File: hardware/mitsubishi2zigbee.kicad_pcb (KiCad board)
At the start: 2 copper layers, 10 parts, among them J1 CN105, Q1 BSS138, Q2 BSS138

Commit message: refactor(kicad-pcb): tweak plot configuration and output directory
- update layerselection and plot_on_all_layers_selection masks
- adjust PDF metadata and popup settings
- modify outputdirectory to target location
- change drillshape, mirror, and outputformat values
- relocate drawing element to Edge.Cuts layer with new UUID
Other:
- board outline added: 30 x 45 mm
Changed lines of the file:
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@@
 		(filling no)
 		(pcbplotparams
-			(layerselection 0x00000000_00000000_55555555_5755f5ff)
-			(plot_on_all_layers_selection 0x00000000_00000000_00000000_00000000)
+			(layerselection 0x00000000_00000000_55555555_55555551)
+			(plot_on_all_layers_selection 0x00000000_00000000_00000000_02000000)
 			(disableapertmacros no)
 			(usegerberextensions no)
@@
 			(mode 1)
 			(useauxorigin no)
-			(pdf_front_fp_property_popups yes)
-			(pdf_back_fp_property_popups yes)
-			(pdf_metadata yes)
-			(pdf_single_document no)
+			(pdf_front_fp_property_popups no)
+			(pdf_back_fp_property_popups no)
+			(pdf_metadata no)
+			(pdf_single_document yes)
 			(dxfpolygonmode yes)
 			(dxfimperialunits yes)
@@
 			(crossoutdnponfab yes)
 			(subtractmaskfromsilk no)
-			(outputformat 1)
-			(mirror no)
-			(drillshape 1)
+			(outputformat 4)
+			(mirror yes)
+			(drillshape 0)
 			(scaleselection 1)
-			(outputdirectory "")
+			(outputdirectory "/home/cleboost/Downloads/")
 		)
 	)
@@
 	)
 	(gr_rect
-		(start 110 30)
-		(end 140 75)
+		(start 111 30.5)
+		(end 141 75.5)
 		(stroke
 			(width 0.1)
@@
 		)
 		(fill no)
-		(layer "Dwgs.User")
+		(layer "Edge.Cuts")
 	)
 	(segment

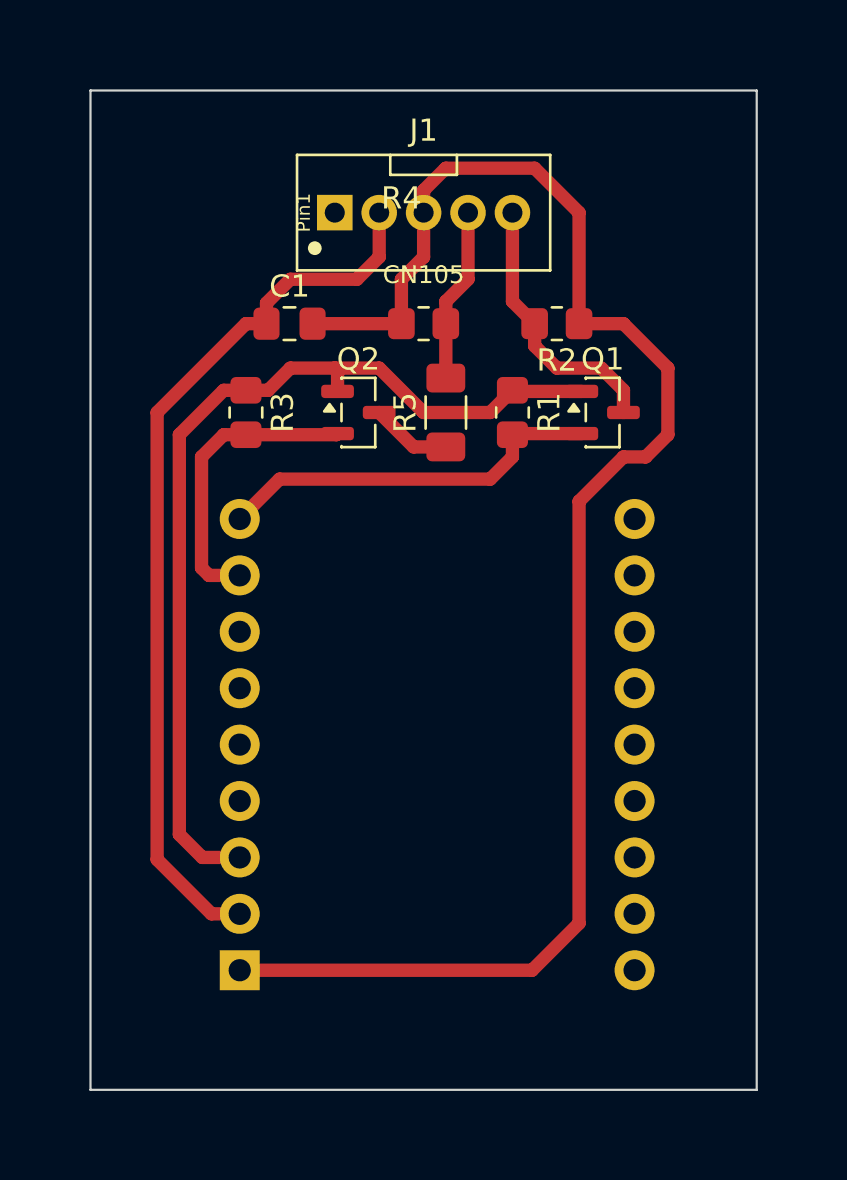
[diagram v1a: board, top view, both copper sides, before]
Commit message: fix(pcb): correct U1 pitch to 15.24mm and adapt pads for DIY etching/drilling
- Correct ESP32-C6-Zero footprint pitch from 17.78mm to official 15.24mm
- Reroute VCC trace around pin headers to ensure proper clearance
- Enlarge U1 pads to 2.1mm (0.9mm drill) for manual Dremel drilling
- Enlarge J1 pads to 1.5x2.2mm oval (0.8mm drill) and add 1.1mm boss hole
- Maintain 100% single-face F.Cu routing with 0 DRC/ERC errors
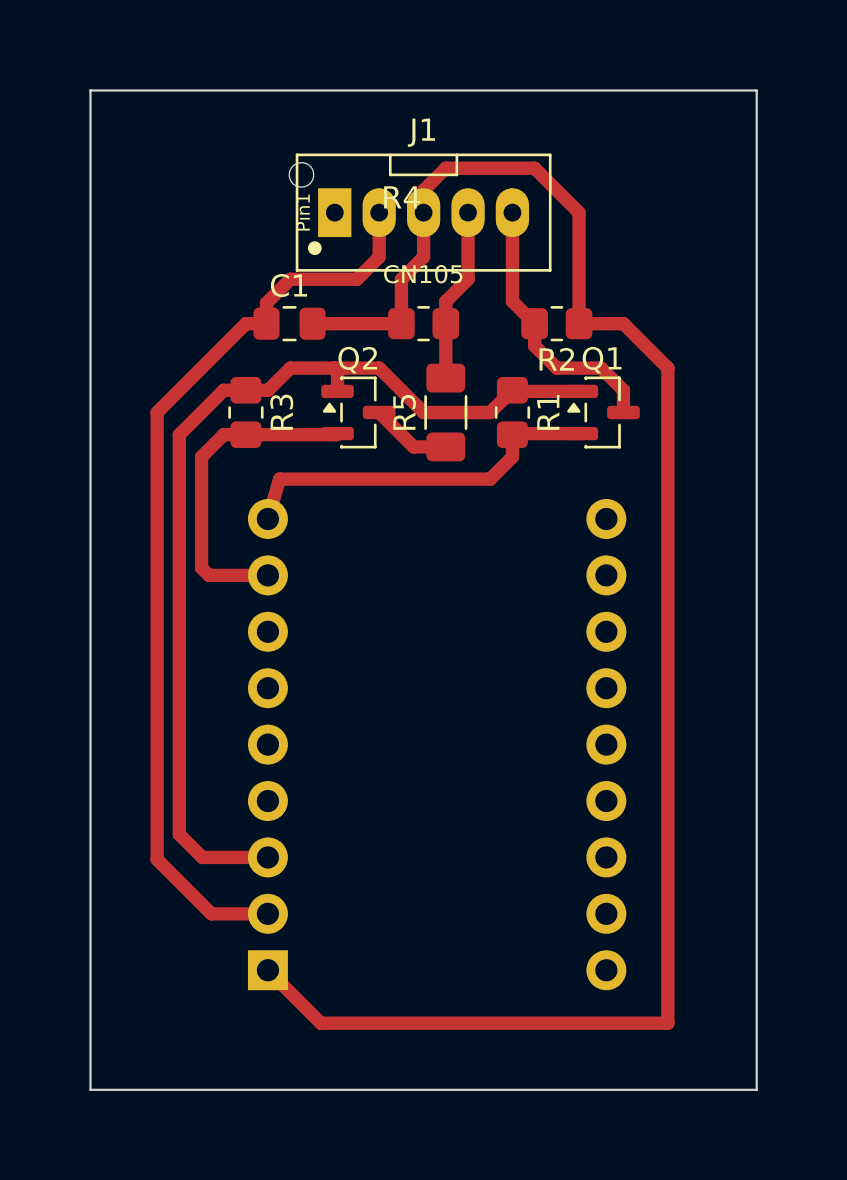
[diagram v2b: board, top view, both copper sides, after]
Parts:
- U1: value ~ -> ESP32-C6-Zero
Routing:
- net VCC: track 72.3 -> 77.4 mm
- net GND: track 40.4 -> 41.6 mm
- net /TX_3V3: track 13.4 -> 14.7 mm
- net +3V3: track 43.0 -> 44.2 mm
- net /RX_3V3: track 17.6 -> 16.9 mm
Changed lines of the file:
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@@
 			)
+		)
+		(pad "" np_thru_hole circle
+			(at -1.5 -1.7)
+			(size 1.1 1.1)
+			(drill 1.1)
+			(layers "*.Cu" "*.Mask")
 		)
 		(pad "1" thru_hole rect
 			(at 0 0)
-			(size 1.6 1.6)
-			(drill 0.9)
+			(size 1.5 2.2)
+			(drill 0.8)
 			(layers "*.Cu" "*.Mask")
 			(remove_unused_layers no)
@@
 		(pad "2" thru_hole oval
 			(at 2 0)
-			(size 1.6 1.6)
-			(drill 0.9)
+			(size 1.5 2.2)
+			(drill 0.8)
 			(layers "*.Cu" "*.Mask")
 			(remove_unused_layers no)
@@
 		(pad "3" thru_hole oval
 			(at 4 0)
-			(size 1.6 1.6)
-			(drill 0.9)
+			(size 1.5 2.2)
+			(drill 0.8)
 			(layers "*.Cu" "*.Mask")
 			(remove_unused_layers no)
@@
 		(pad "4" thru_hole oval
 			(at 6 0)
-			(size 1.6 1.6)
-			(drill 0.9)
+			(size 1.5 2.2)
+			(drill 0.8)
 			(layers "*.Cu" "*.Mask")
 			(remove_unused_layers no)
@@
 		(pad "5" thru_hole oval
 			(at 8 0)
-			(size 1.6 1.6)
-			(drill 0.9)
+			(size 1.5 2.2)
+			(drill 0.8)
 			(layers "*.Cu" "*.Mask")
 			(remove_unused_layers no)
@@
 			)
 		)
-		(property "Value" "~"
+		(property "Value" "ESP32-C6-Zero"
 			(at 0 -25 0)
 			(layer "B.Fab")
@@
 		)
 		(pad "1" thru_hole rect
-			(at -8.89 0)
+			(at -7.62 0)
 			(size 1.8 1.8)
 			(drill 1)
@@
 		)
 		(pad "2" thru_hole circle
-			(at -8.89 -2.54)
+			(at -7.62 -2.54)
 			(size 1.8 1.8)
 			(drill 1)
@@
 		)
 		(pad "3" thru_hole circle
-			(at -8.89 -5.08)
+			(at -7.62 -5.08)
 			(size 1.8 1.8)
 			(drill 1)
@@
 		)
 		(pad "4" thru_hole circle
-			(at -8.89 -7.62)
+			(at -7.62 -7.62)
 			(size 1.8 1.8)
 			(drill 1)
@@
 		)
 		(pad "5" thru_hole circle
-			(at -8.89 -10.16)
+			(at -7.62 -10.16)
 			(size 1.8 1.8)
 			(drill 1)
@@
 		)
 		(pad "6" thru_hole circle
-			(at -8.89 -12.7)
+			(at -7.62 -12.7)
 			(size 1.8 1.8)
 			(drill 1)
@@
 		)
 		(pad "7" thru_hole circle
-			(at -8.89 -15.24)
+			(at -7.62 -15.24)
 			(size 1.8 1.8)
 			(drill 1)
@@
 		)
 		(pad "8" thru_hole circle
-			(at -8.89 -17.78)
+			(at -7.62 -17.78)
 			(size 1.8 1.8)
 			(drill 1)
@@
 		)
 		(pad "9" thru_hole circle
-			(at -8.89 -20.32)
+			(at -7.62 -20.32)
 			(size 1.8 1.8)
 			(drill 1)
@@
 		)
 		(pad "10" thru_hole circle
-			(at 8.89 -20.32)
+			(at 7.62 -20.32)
 			(size 1.8 1.8)
 			(drill 1)
@@
 		)
 		(pad "11" thru_hole circle
-			(at 8.89 -17.78)
+			(at 7.62 -17.78)
 			(size 1.8 1.8)
 			(drill 1)
@@
 		)
 		(pad "12" thru_hole circle
-			(at 8.89 -15.24)
+			(at 7.62 -15.24)
 			(size 1.8 1.8)
 			(drill 1)
@@
 		)
 		(pad "13" thru_hole circle
-			(at 8.89 -12.7)
+			(at 7.62 -12.7)
 			(size 1.8 1.8)
 			(drill 1)
@@
 		)
 		(pad "14" thru_hole circle
-			(at 8.89 -10.16)
+			(at 7.62 -10.16)
 			(size 1.8 1.8)
 			(drill 1)
@@
 		)
 		(pad "15" thru_hole circle
-			(at 8.89 -7.62)
+			(at 7.62 -7.62)
 			(size 1.8 1.8)
 			(drill 1)
@@
 		)
 		(pad "16" thru_hole circle
-			(at 8.89 -5.08)
+			(at 7.62 -5.08)
 			(size 1.8 1.8)
 			(drill 1)
@@
 		)
 		(pad "17" thru_hole circle
-			(at 8.89 -2.54)
+			(at 7.62 -2.54)
 			(size 1.8 1.8)
 			(drill 1)
@@
 		)
 		(pad "18" thru_hole circle
-			(at 8.89 0)
+			(at 7.62 0)
 			(size 1.8 1.8)
 			(drill 1)
@@
 	)
 	(segment
-		(start 117.72 65.035)
+		(start 118.99 65.035)
 		(end 116.035 65.035)
 		(width 0.6)
@@
 	(segment
 		(start 119.515 48)
-		(end 117.72 49.795)
+		(end 118.99 49.795)
 		(width 0.6)
 		(layer "F.Cu")
@@
 	)
 	(segment
+		(start 137 43)
+		(end 137 72.5)
+		(width 0.6)
+		(layer "F.Cu")
+		(net "VCC")
+	)
+	(segment
 		(start 121 41)
 		(end 125 41)
@@
 	)
 	(segment
-		(start 135 47)
-		(end 136 47)
+		(start 125 41)
+		(end 124.73 40.73)
+		(width 0.6)
+		(layer "F.Cu")
+		(net "VCC")
+	)
+	(segment
+		(start 125 39)
+		(end 125 41)
+		(width 0.6)
+		(layer "F.Cu")
+		(net "VCC")
+	)
+	(segment
+		(start 126 38)
+		(end 125 39)
+		(width 0.6)
+		(layer "F.Cu")
+		(net "VCC")
+	)
+	(segment
+		(start 131 34)
+		(end 127 34)
+		(width 0.6)
+		(layer "F.Cu")
+		(net "VCC")
+	)
+	(segment
+		(start 135 41)
+		(end 137 43)
+		(width 0.6)
+		(layer "F.Cu")
+		(net "VCC")
+	)
+	(segment
+		(start 133 36)
+		(end 131 34)
+		(width 0.6)
+		(layer "F.Cu")
+		(net "VCC")
+	)
+	(segment
+		(start 126 35)
+		(end 127 34)
 		(width 0.6)
 		(layer "F.Cu")
@@
 	)
 	(segment
-		(start 133 49)
-		(end 133 68)
+		(start 137 72.5)
+		(end 121.375 72.5)
 		(width 0.6)
 		(layer "F.Cu")
@@
 	)
 	(segment
-		(start 135 41)
-		(end 137 43)
-		(width 0.6)
-		(layer "F.Cu")
-		(net "VCC")
-	)
-	(segment
-		(start 125 41)
-		(end 124.73 40.73)
-		(width 0.6)
-		(layer "F.Cu")
-		(net "VCC")
-	)
-	(segment
-		(start 125 39)
-		(end 125 41)
-		(width 0.6)
-		(layer "F.Cu")
-		(net "VCC")
-	)
-	(segment
-		(start 137 43)
-		(end 137 46)
-		(width 0.6)
-		(layer "F.Cu")
-		(net "VCC")
-	)
-	(segment
-		(start 133 68)
-		(end 130.885 70.115)
-		(width 0.6)
-		(layer "F.Cu")
-		(net "VCC")
-	)
-	(segment
-		(start 126 38)
-		(end 125 39)
-		(width 0.6)
-		(layer "F.Cu")
-		(net "VCC")
-	)
-	(segment
-		(start 136 47)
-		(end 137 46)
-		(width 0.6)
-		(layer "F.Cu")
-		(net "VCC")
-	)
-	(segment
-		(start 131 34)
-		(end 127 34)
-		(width 0.6)
-		(layer "F.Cu")
-		(net "VCC")
-	)
-	(segment
-		(start 133 36)
-		(end 131 34)
-		(width 0.6)
-		(layer "F.Cu")
-		(net "VCC")
-	)
-	(segment
-		(start 126 35)
-		(end 127 34)
-		(width 0.6)
-		(layer "F.Cu")
-		(net "VCC")
-	)
-	(segment
-		(start 130.885 70.115)
-		(end 117.72 70.115)
+		(start 121.375 72.5)
+		(end 118.99 70.115)
 		(width 0.6)
 		(layer "F.Cu")
@@
 	)
 	(segment
-		(start 133 49)
-		(end 135 47)
-		(width 0.6)
-		(layer "F.Cu")
-		(net "VCC")
-	)
-	(segment
 		(start 133 41)
 		(end 133 36)
@@
 	)
 	(segment
-		(start 117.72 52.335)
+		(start 118.99 52.335)
 		(end 116.335 52.335)
 		(width 0.6)
@@
 	)
 	(segment
-		(start 117.72 67.575)
+		(start 118.99 67.575)
 		(end 116.447208 67.575)
 		(width 0.6)

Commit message: feat(hardware): add ready-to-print DIY etching typon with alignment marks and Cu text
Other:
- board text added: "F.Cu"
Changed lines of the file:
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@@
 		(layer "Edge.Cuts")
+	)
+	(gr_rect
+		(start 111 30.5)
+		(end 141 75.5)
+		(stroke
+			(width 0.2)
+			(type default)
+		)
+		(fill no)
+		(layer "F.Cu")
+	)
+	(gr_line
+		(start 109 30.5)
+		(end 113 30.5)
+		(stroke
+			(width 0.15)
+			(type default)
+		)
+		(layer "F.Cu")
+	)
+	(gr_line
+		(start 111 28.5)
+		(end 111 32.5)
+		(stroke
+			(width 0.15)
+			(type default)
+		)
+		(layer "F.Cu")
+	)
+	(gr_line
+		(start 139 30.5)
+		(end 143 30.5)
+		(stroke
+			(width 0.15)
+			(type default)
+		)
+		(layer "F.Cu")
+	)
+	(gr_line
+		(start 141 28.5)
+		(end 141 32.5)
+		(stroke
+			(width 0.15)
+			(type default)
+		)
+		(layer "F.Cu")
+	)
+	(gr_line
+		(start 109 75.5)
+		(end 113 75.5)
+		(stroke
+			(width 0.15)
+			(type default)
+		)
+		(layer "F.Cu")
+	)
+	(gr_line
+		(start 111 73.5)
+		(end 111 77.5)
+		(stroke
+			(width 0.15)
+			(type default)
+		)
+		(layer "F.Cu")
+	)
+	(gr_line
+		(start 139 75.5)
+		(end 143 75.5)
+		(stroke
+			(width 0.15)
+			(type default)
+		)
+		(layer "F.Cu")
+	)
+	(gr_line
+		(start 141 73.5)
+		(end 141 77.5)
+		(stroke
+			(width 0.15)
+			(type default)
+		)
+		(layer "F.Cu")
+	)
+	(gr_text "F.Cu"
+		(at 137.5 33 0)
+		(layer "F.Cu")
+		(effects
+			(font
+				(size 1.2 1.2)
+				(thickness 0.2)
+			)
+		)
 	)
 	(segment
